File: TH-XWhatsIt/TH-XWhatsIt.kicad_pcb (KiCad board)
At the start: 2 copper layers, 178 x 115.5 mm, 37 parts, among them J1 COLUMNS, J10 DISPLAYWRITER PLUGBOARD CONNE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, J11 DISPLAYWRITER PLUGBOARD ROWS, J12 EXPANSION HEADER, J2 ROWS, J3 MODEL F PLUGBOARD COLUMNS, J4 MODEL F PLUGBOARD CONNECTOR, J5 MODEL F PLUGBOARD ROWS, J6 BEAMSPRING PLUGBOARD COLUMNS, J7 BEAMSPRING PLUGBOARD CONNECTOR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

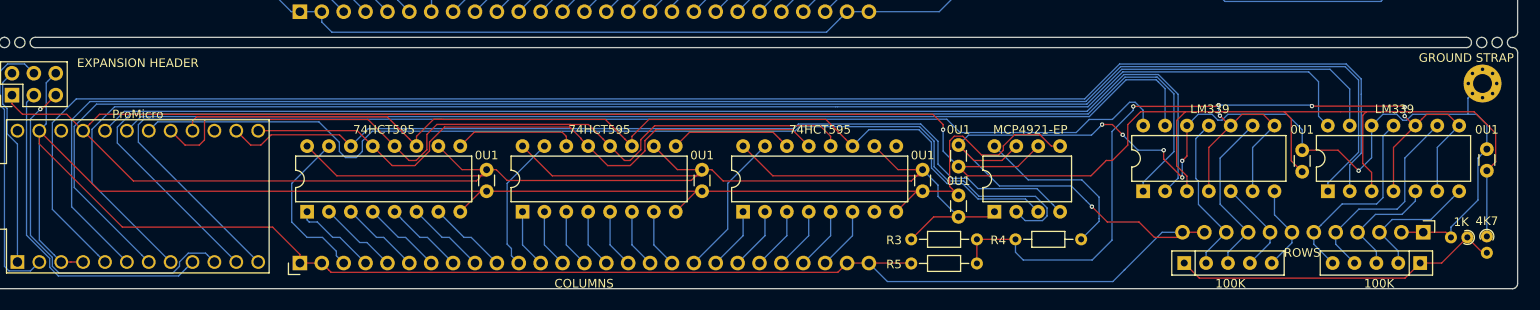
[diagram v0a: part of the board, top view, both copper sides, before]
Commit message: Add option to use individual resistors to pull towards bias
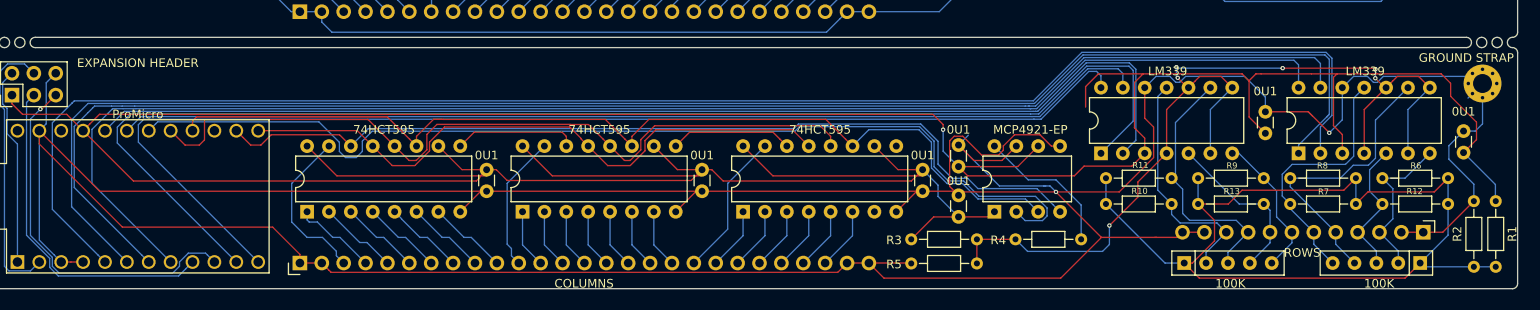
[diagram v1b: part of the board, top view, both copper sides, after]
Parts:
- added R10: NM, Resistor_THT:R_Axial_DIN0204_L3.6mm_D1.6mm_P7.62mm_Horizontal, F.Cu at (183.8, 139.0)
- added R11: NM, Resistor_THT:R_Axial_DIN0204_L3.6mm_D1.6mm_P7.62mm_Horizontal, F.Cu at (183.8, 136.0)
- added R12: NM, Resistor_THT:R_Axial_DIN0204_L3.6mm_D1.6mm_P7.62mm_Horizontal, F.Cu at (223.5, 139.0)
- added R13: NM, Resistor_THT:R_Axial_DIN0204_L3.6mm_D1.6mm_P7.62mm_Horizontal, F.Cu at (194.5, 139.0)
- added R6: NM, Resistor_THT:R_Axial_DIN0204_L3.6mm_D1.6mm_P7.62mm_Horizontal, F.Cu at (223.5, 136.0)
- added R7: NM, Resistor_THT:R_Axial_DIN0204_L3.6mm_D1.6mm_P7.62mm_Horizontal, F.Cu at (212.8, 139.0)
- added R8: NM, Resistor_THT:R_Axial_DIN0204_L3.6mm_D1.6mm_P7.62mm_Horizontal, F.Cu at (212.8, 136.0)
- added R9: NM, Resistor_THT:R_Axial_DIN0204_L3.6mm_D1.6mm_P7.62mm_Horizontal, F.Cu at (194.5, 136.0)
- R1, R2: footprint Resistor_THT:R_Axial_DIN0204_L3.6mm_D1.6mm_P1.90mm_Vertical -> Resistor_THT:R_Axial_DIN0204_L3.6mm_D1.6mm_P7.62mm_Horizontal
- moved U6 6.59 mm to (183.2, 133.1)
- moved C10 6.17 mm to (202.3, 128.3)
- moved U1 5.56 mm to (206.2, 133.1)
- moved R1 4.22 mm to (229.0, 138.7)
- moved R2 3.50 mm to (226.5, 146.3), turned to 90 degrees
- moved C9 3.42 mm to (225.3, 130.5)
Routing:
- net BIAS: track 38.5 -> 111.0 mm
- net SETPOINT: track 122.3 -> 108.6 mm
- net SENSE6: track 19.8 -> 30.0 mm
- net SENSE3: track 24.3 -> 33.5 mm
- net SENSE8: track 19.0 -> 27.6 mm
- net SENSE7: track 11.2 -> 19.5 mm
- net SENSE4: track 23.0 -> 30.3 mm
- net ROW8: track 127.7 -> 120.4 mm
- net SENSE5: track 10.1 -> 17.0 mm
- net ROW7: track 140.1 -> 133.6 mm
- net ROW5: track 160.0 -> 153.6 mm
- net ROW6: track 142.8 -> 137.6 mm
- net ROW2: track 187.7 -> 182.5 mm
- net +5VA: track 445.9 -> 451.0 mm
- net ROW4: track 175.3 -> 170.4 mm
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
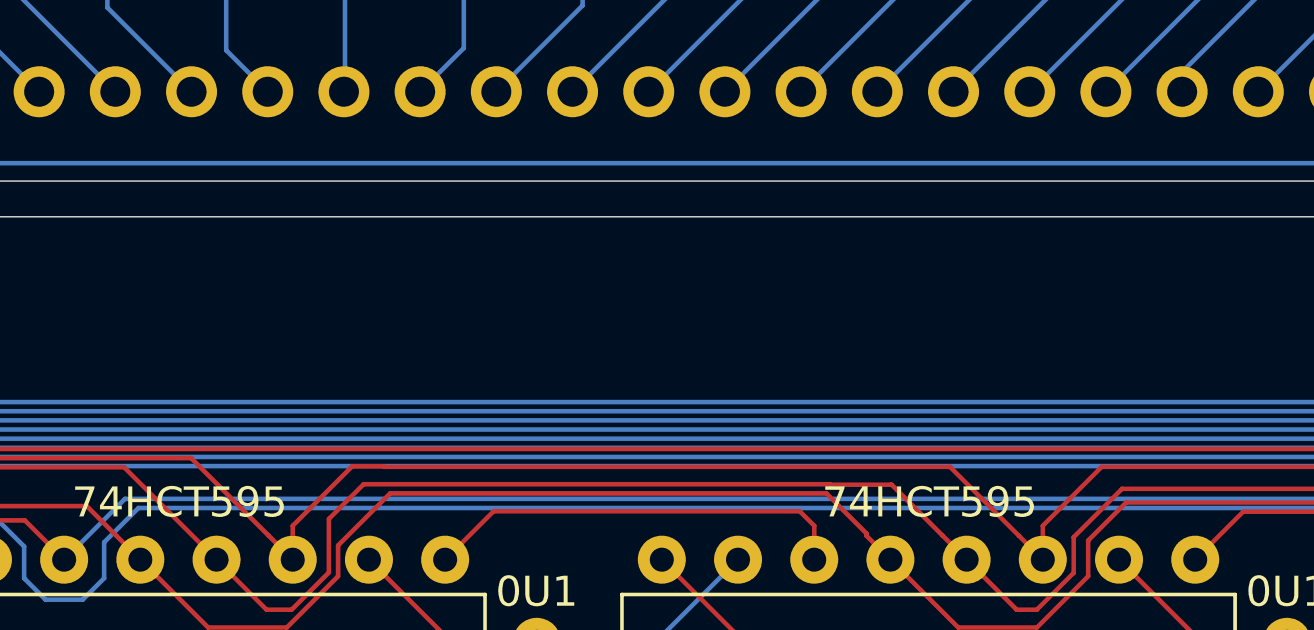
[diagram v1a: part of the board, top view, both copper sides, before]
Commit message: Renamed schematic title form THT-Xwhatsit to TH xwhatsit, bumped revision to 0.0.3, added revision to silkscreen, added changelog
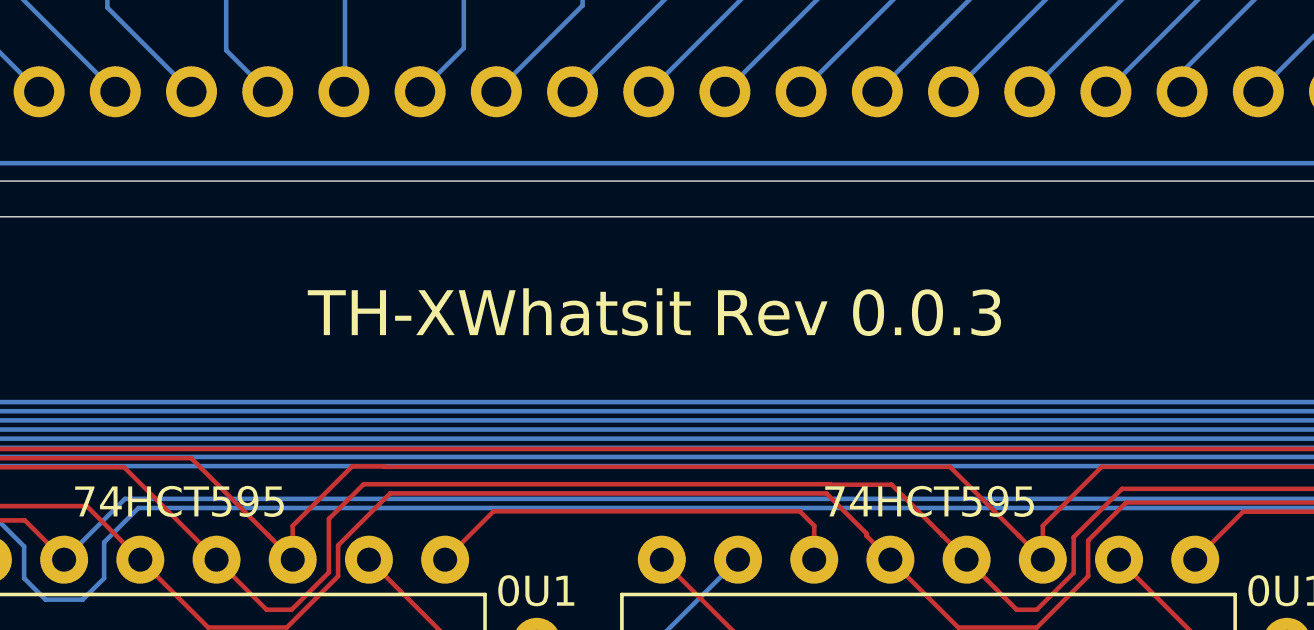
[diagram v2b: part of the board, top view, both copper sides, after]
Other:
- board text added: "TH-XWhatsit Rev 0.0.3"

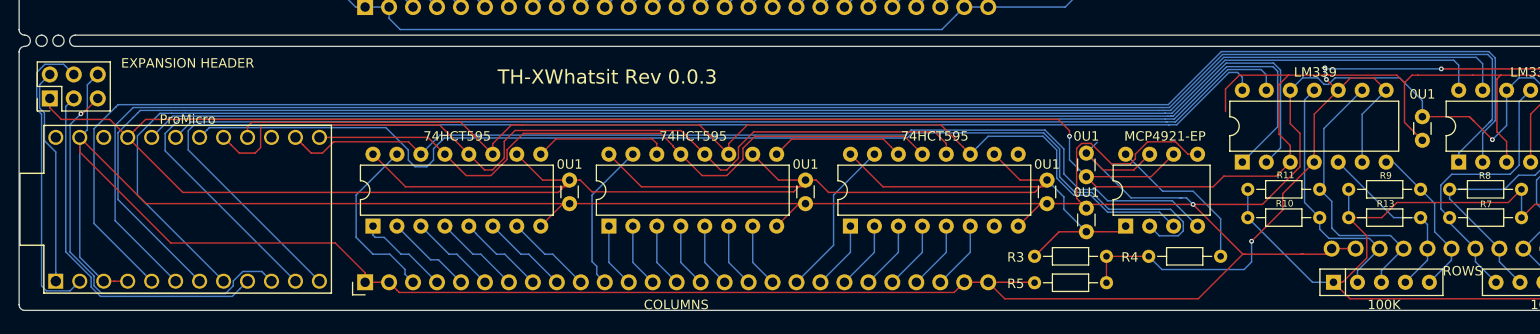
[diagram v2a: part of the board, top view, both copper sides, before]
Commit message: Added pads to short reset on bottom
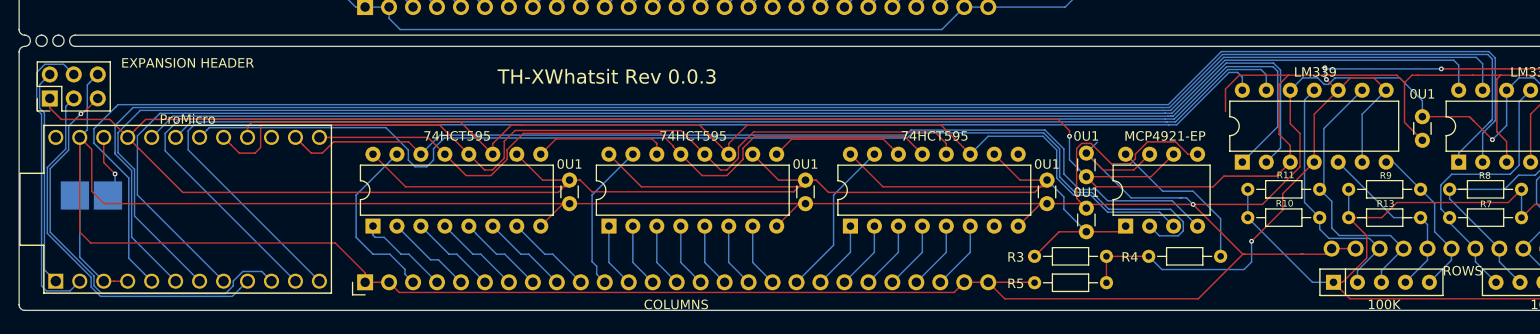
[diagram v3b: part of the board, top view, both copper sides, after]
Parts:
- added J13: Conn_01x02, TH-XWhatsIt:PadsToShort, B.Cu at (61.2, 139.5)
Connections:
- U7 pad 22: Net-(U7-Pad22) -> RESET
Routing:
- net GNDA: track 467.2 -> 475.2 mm
- net RESET: track 0.00 -> 6.97 mm, vias 0 -> 1
- net HEADER2: track 43.1 -> 44.8 mm
- net HEADER1: track 39.1 -> 40.7 mm
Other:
- board text added: "GND"
- board text added: "RST"

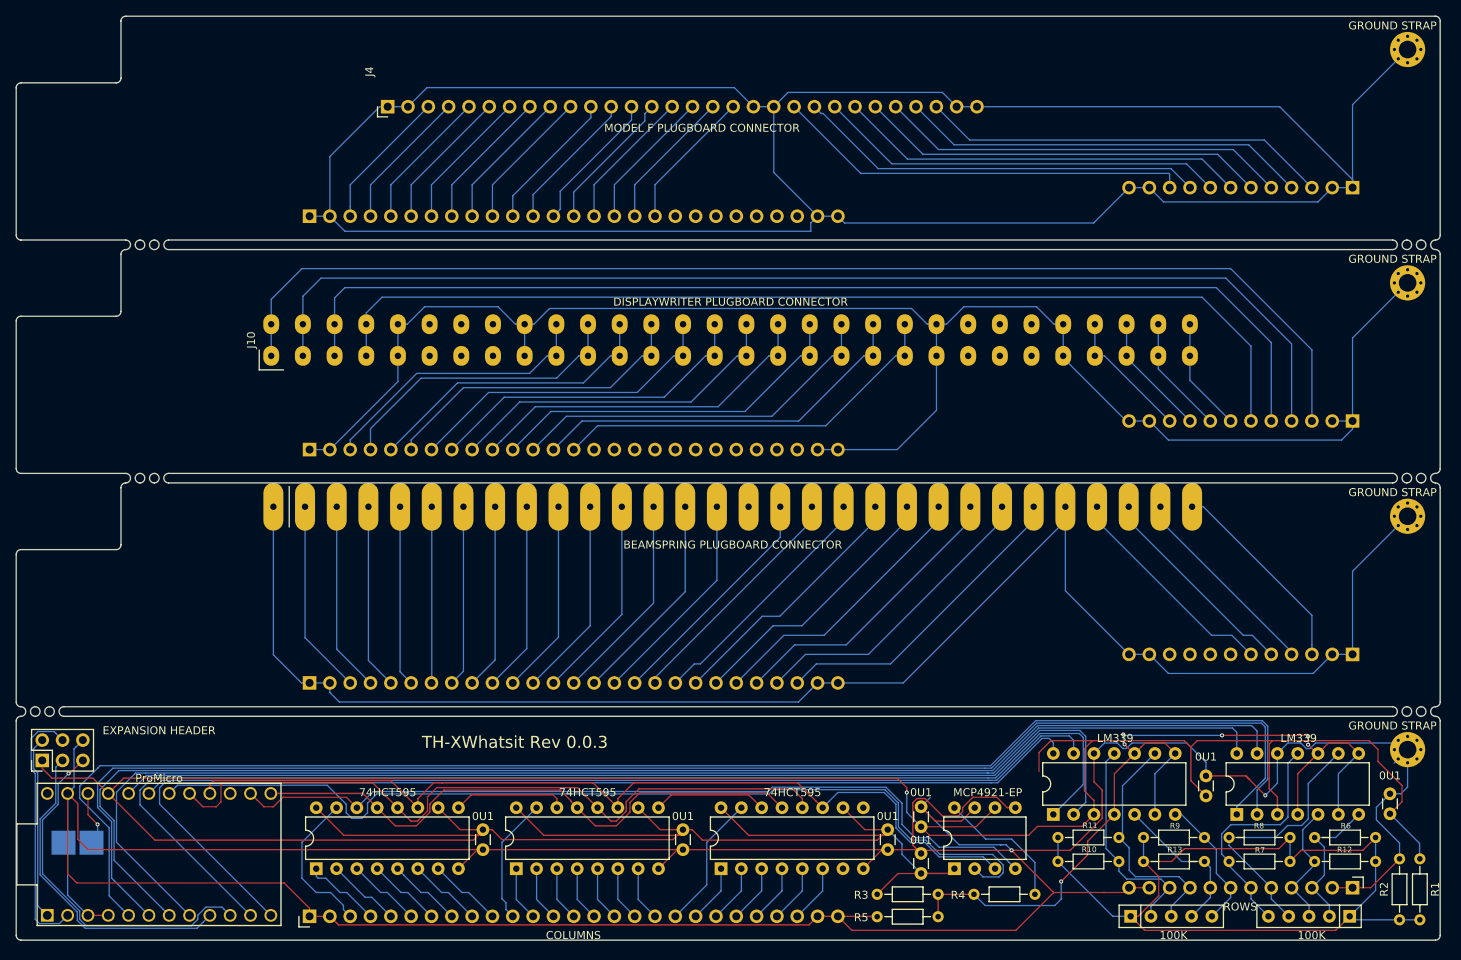
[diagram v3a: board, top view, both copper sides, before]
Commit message: Use net tie to enforce star ground on the controller
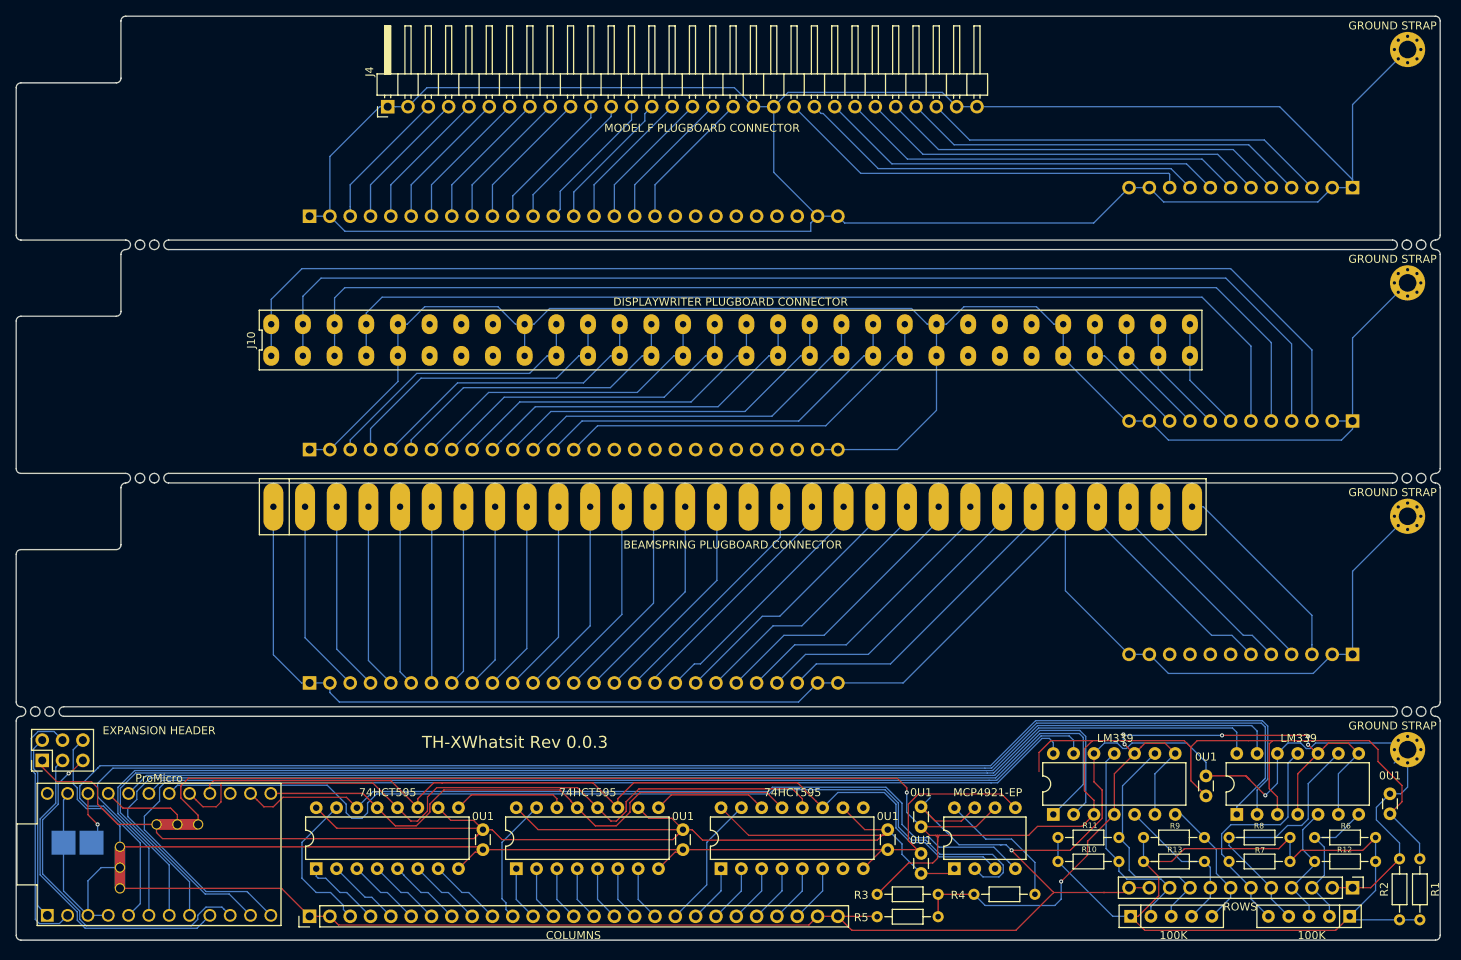
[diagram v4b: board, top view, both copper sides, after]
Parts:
- added NT1: Net-Tie_3, NetTie:NetTie-3_THT_Pad1.0mm, F.Cu at (66.5, 137.2)
- added NT2: Net-Tie_3, NetTie:NetTie-3_THT_Pad1.0mm, F.Cu at (71.1, 134.4)
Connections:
- C3 pad 1: GNDA -> GNDD
- C3 pad 2: +5VA -> +5VD
- C5 pad 1: GNDA -> GNDD
- C5 pad 2: +5VA -> +5VD
- C7 pad 1: GNDA -> GNDD
- C7 pad 2: +5VA -> +5VD
- C8 pad 1: GNDA -> GNDD
- C8 pad 2: +5VA -> +5VD
- J12 pad 1: +5VA -> +5VD
- J12 pad 6: GNDA -> GNDD
- J13 pad 1: GNDA -> GND
- U2 pad 1: +5VA -> +5VD
- U2 pad 5: GNDA -> GNDD
- U3 pad 10: +5VA -> +5VD
- U3 pad 16: +5VA -> +5VD
- U3 pad 8: GNDA -> GNDD
- U5 pad 10: +5VA -> +5VD
- U5 pad 16: +5VA -> +5VD
- U5 pad 8: GNDA -> GNDD
- U7 pad 21: +5VA -> VCC
- U7 pad 23: GNDA -> GND
- U7 pad 3: GNDA -> GND
- U7 pad 4: GNDA -> GND
- U8 pad 10: +5VA -> +5VD
- U8 pad 16: +5VA -> +5VD
- U8 pad 8: GNDA -> GNDD
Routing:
- net +5VD: track 0.00 -> 216.0 mm
- net +5VA: track 451.0 -> 240.5 mm
- net GNDA: track 475.2 -> 272.1 mm
- net GNDD: track 0.00 -> 152.6 mm
- net GND: track 0.00 -> 29.4 mm
- net VCC: track 0.00 -> 10.9 mm
- net ROW6: track 137.6 -> 142.1 mm
- net ROW5: track 153.6 -> 156.8 mm
- net ROW4: track 170.4 -> 167.4 mm
- net ROW2: track 182.5 -> 184.9 mm

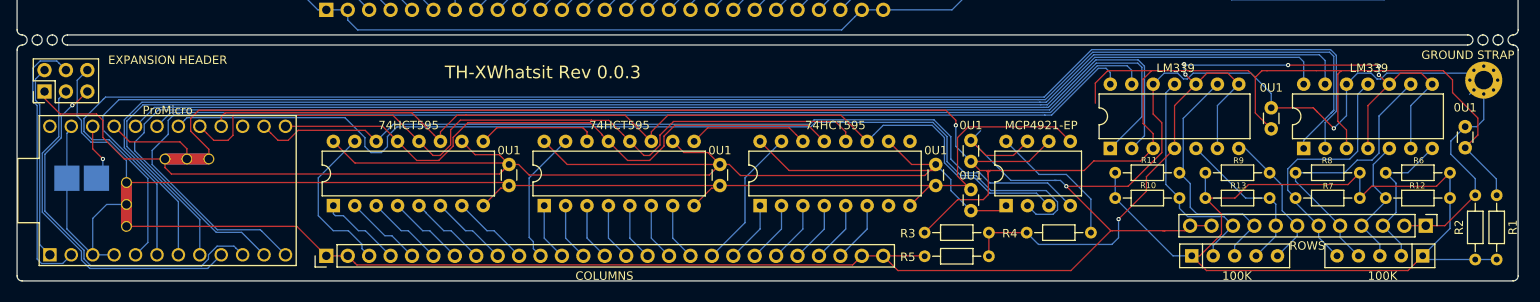
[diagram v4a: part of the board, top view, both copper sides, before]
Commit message: thicken up ground traces
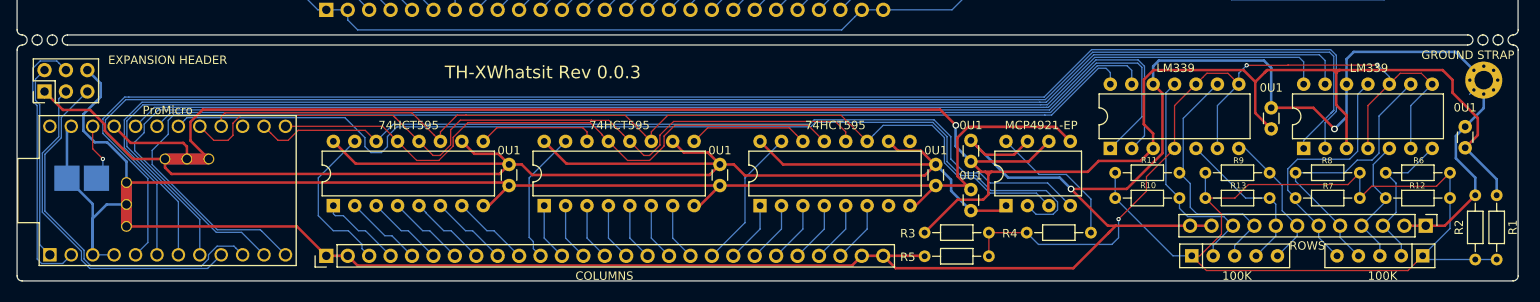
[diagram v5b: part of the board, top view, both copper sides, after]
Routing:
- net GNDD: track 152.6 -> 199.0 mm
- net +5VA: track 240.5 -> 231.0 mm
- net SETPOINT: track 108.6 -> 100.7 mm, vias 6 -> 3
- net GND: track 29.4 -> 35.8 mm
- net ROW2: track 184.9 -> 180.5 mm
- net GNDA: track 272.1 -> 276.3 mm
- net +5VD: track 216.0 -> 218.7 mm
- net ROW1: track 181.3 -> 180.5 mm
- net HEADER2: track 44.8 -> 44.7 mm, vias 1 -> 0
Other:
- net class Power added: clearance 0.1524, trace_width 0.3048, via_dia 0.8, via_drill 0.5
